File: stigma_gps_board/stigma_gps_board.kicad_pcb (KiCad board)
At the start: 2 copper layers, 40 x 40 mm, 18 parts, among them J1 DF40GB-70DP-0.4V, U1 NCP115AMX120TCG, U2 SAM-M10Q

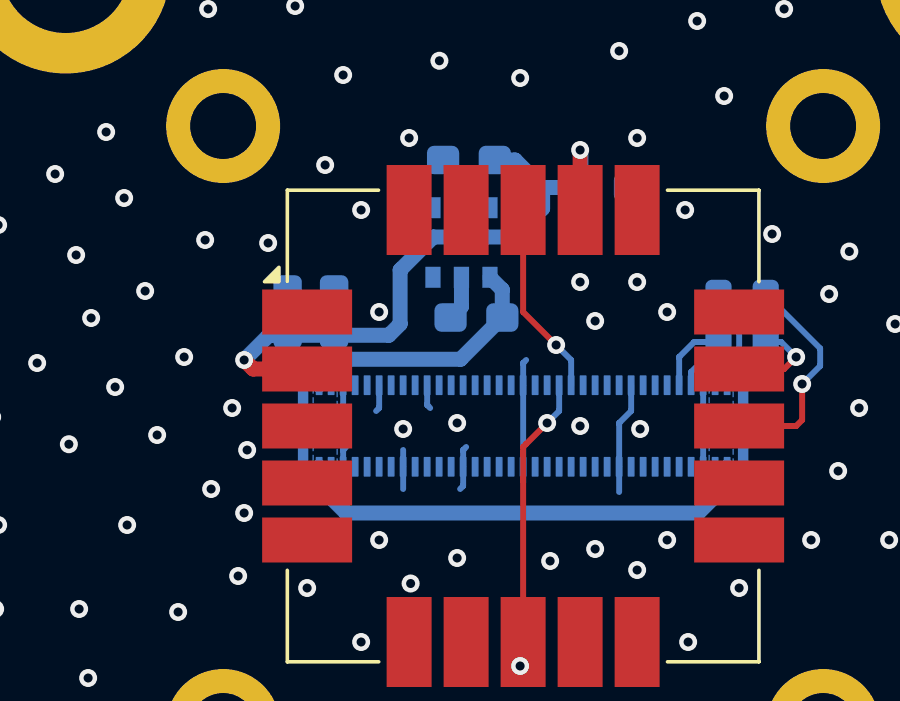
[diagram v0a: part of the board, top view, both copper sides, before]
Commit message: fix voltage regulator
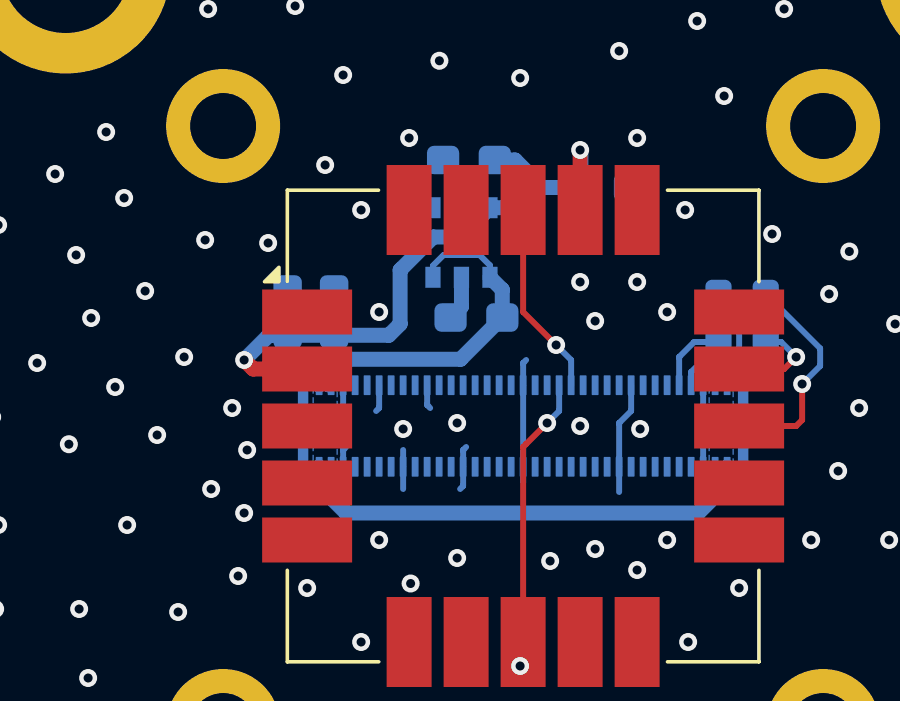
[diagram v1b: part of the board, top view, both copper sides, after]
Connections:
- U1 pad 3: unconnected-(U1-EN-Pad3) -> +5V
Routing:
- net +5V: track 24.4 -> 28.0 mm

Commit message: increase ref to 2
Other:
- board text added: "rev 2"
- board text removed: "rev 1"
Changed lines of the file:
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@@
 		(layer "Edge.Cuts")
 	)
-	(gr_text "rev 1"
+	(gr_text "rev 2"
 		(at 103.95 80.125 0)
 		(layer "F.Mask")

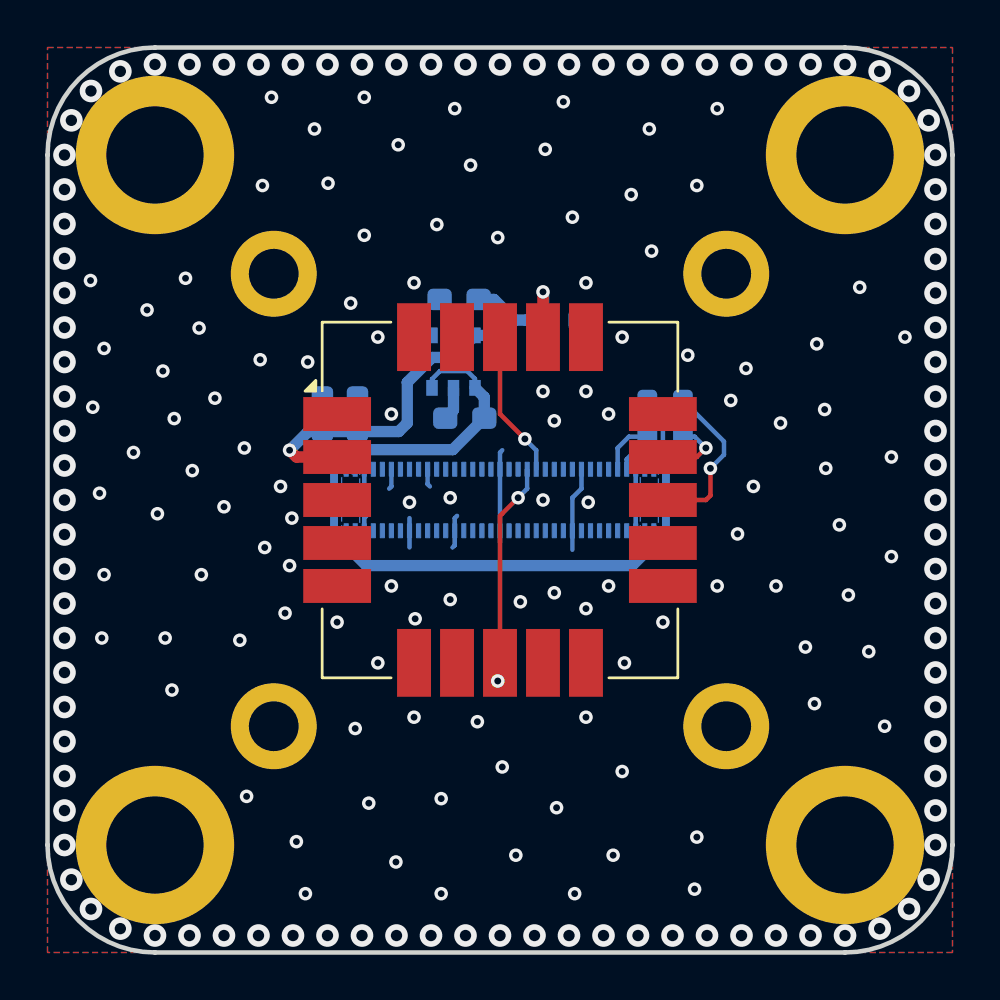
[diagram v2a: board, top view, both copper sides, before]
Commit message: some lcsc number changes
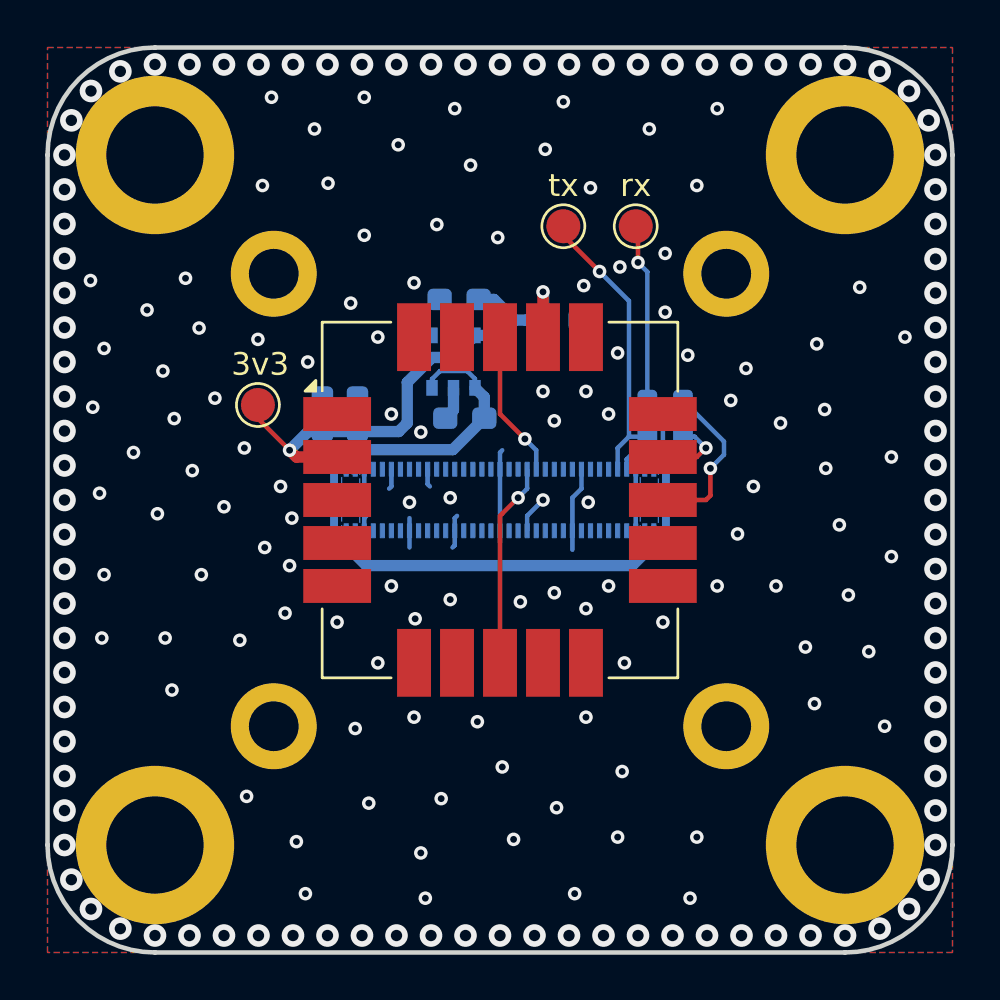
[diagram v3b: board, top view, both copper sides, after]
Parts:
- added TP1: tx, TestPoint:TestPoint_Pad_D1.5mm, F.Cu at (122.8, 57.9)
- added TP2: rx, TestPoint:TestPoint_Pad_D1.5mm, F.Cu at (126.0, 57.9)
- added TP3: 3v3, TestPoint:TestPoint_Pad_D1.5mm, F.Cu at (109.3, 65.8)
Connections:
- U1 pad 4: unconnected-(U1-NC-Pad4) -> GND
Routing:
- net UART8_TX_GPS: track 2.46 -> 13.1 mm, vias 0 -> 1
- net UART8_RX_GPS: track 4.57 -> 12.6 mm, vias 0 -> 1
- net +3.3V: track 22.1 -> 24.7 mm
- net GND: track 19.8 -> 21.5 mm, vias 209 -> 210
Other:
- board text added: "rapid gps board"
